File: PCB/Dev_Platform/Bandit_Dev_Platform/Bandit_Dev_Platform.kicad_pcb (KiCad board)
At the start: 4 copper layers, 63.5 x 31.8 mm, 126 parts, among them J12 Conn_01x02_Pin, J5 BNC, J6 BNC, P1 USB_C_Plug_USB2.0, SW1 SW_SPST, U1 AD7253, U10 OPA1664, U11 XC6206PxxxMR, U2 RP2040, U4 NCP164ASNADJT1G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

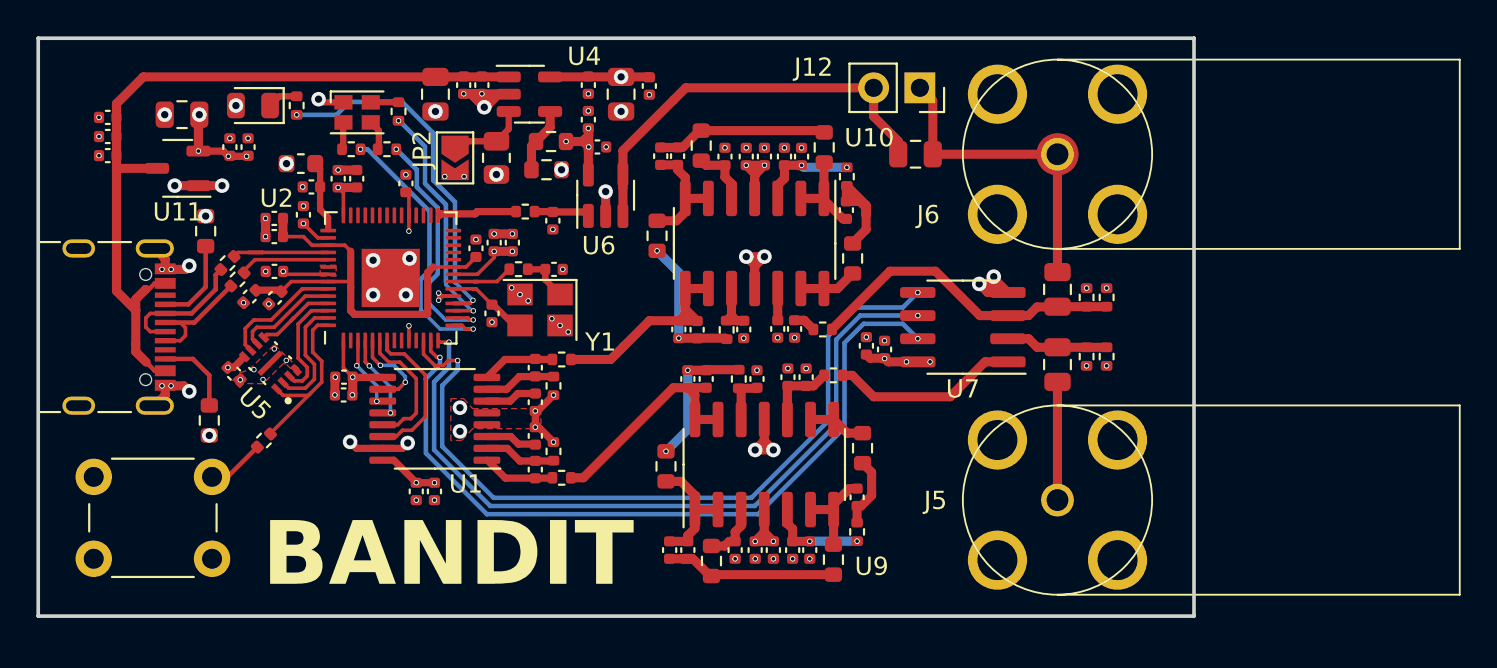
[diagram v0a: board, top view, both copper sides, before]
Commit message: Added filter test board
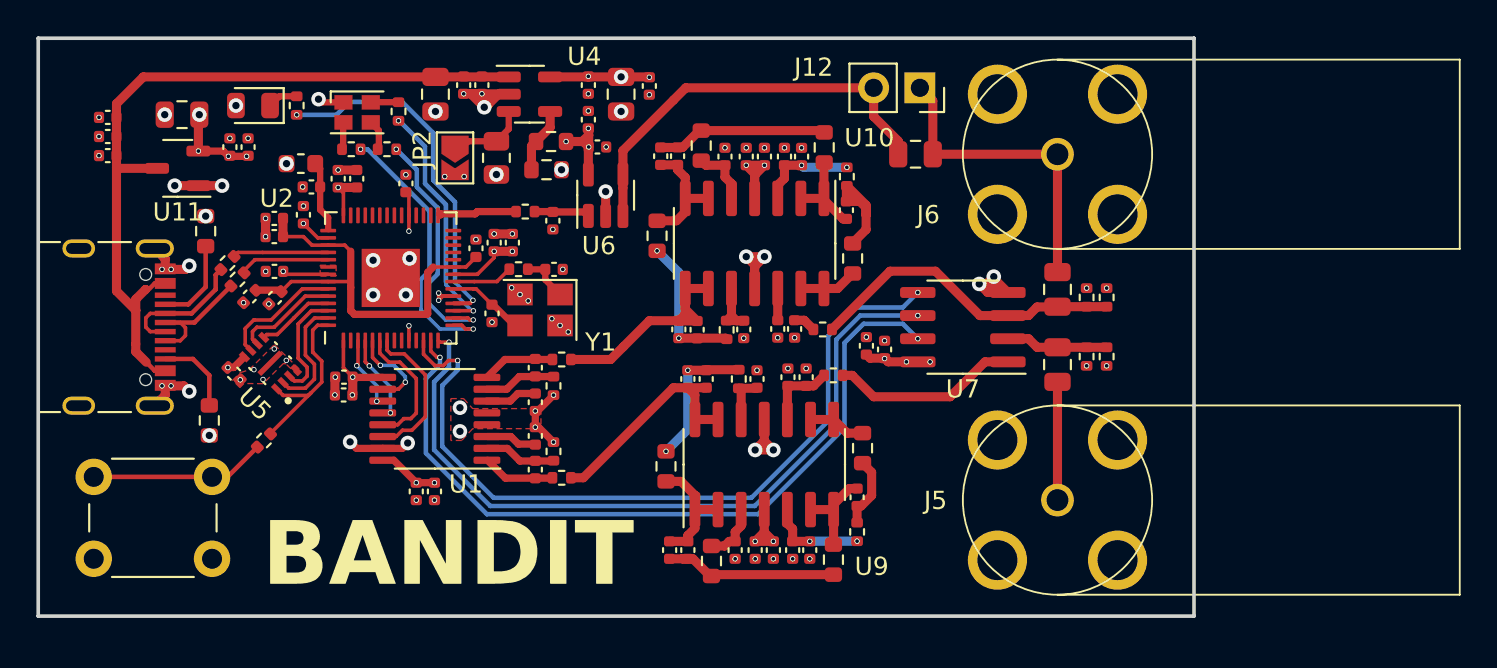
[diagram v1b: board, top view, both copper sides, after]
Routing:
- net GND: track 45.6 -> 59.5 mm
- net Net-(SW1-A): track 3.17 -> 9.67 mm
- net /USB_D-: track 6.04 -> 5.26 mm
- net VDDA: track 25.2 -> 25.3 mm, vias 15 -> 17

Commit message: Dev platform and Filter Test pcb polished, ordered
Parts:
- removed JP2: SolderJumper_2_Open, Jumper:SolderJumper-2_P1.3mm_Open_TrianglePad1.0x1.5mm
- added C12: 100n, Capacitor_SMD:C_0402_1005Metric, F.Cu at (49.7, 41.4)
- added C15: 100n, Capacitor_SMD:C_0402_1005Metric, F.Cu at (49.7, 40.4)
- added C17: 10u, Capacitor_SMD:C_0402_1005Metric, F.Cu at (51.4, 44.1)
- added C18: 10u, Capacitor_SMD:C_0402_1005Metric, F.Cu at (51.4, 37.6)
- added C3: 100n, Capacitor_SMD:C_0402_1005Metric, F.Cu at (68.1, 43.3)
- added C70: 2u2, Capacitor_SMD:C_0402_1005Metric, F.Cu at (39.2, 28.0)
- added R16: 10k, Resistor_SMD:R_0402_1005Metric, F.Cu at (67.6, 41.8)
- added R17: 10k, Resistor_SMD:R_0402_1005Metric, F.Cu at (68.1, 39.3)
- added R18: 10k, Resistor_SMD:R_0402_1005Metric, F.Cu at (51.1, 42.6)
- added R19: 10k, Resistor_SMD:R_0402_1005Metric, F.Cu at (52.1, 42.6)
- added R20: 10k, Resistor_SMD:R_0402_1005Metric, F.Cu at (51.1, 39.1)
- added R42: 10k, Resistor_SMD:R_0402_1005Metric, F.Cu at (51.4, 36.6)
- C2: value 1u -> 10u
- moved C2 30.4 mm to (68.1, 40.3), turned to 0 degrees
- moved SW1 7.85 mm to (27.6, 37.7), turned to -90 degrees
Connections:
- C2 pad 1: VBUS -> /SIG_IN
- C2 pad 2: GND -> Net-(U7-VOUT)
- R22 pad 1: /SE_SIG_A -> Net-(C18-Pad1)
- R23 pad 1: /SE_SIG_B -> Net-(C17-Pad1)
- R7 pad 2: Net-(JP1-B) -> /VDDA_EN
- U2 pad 24: Net-(J1-Pin_1) -> unconnected-(U2-SWCLK-Pad24)
- U2 pad 25: Net-(J1-Pin_2) -> unconnected-(U2-SWD-Pad25)
- U2 pad 32: Net-(J8-Pin_1) -> /VDDA_EN
- U2 pad 34: Net-(J8-Pin_2) -> unconnected-(U2-GPIO22-Pad34)
- U2 pad 35: Net-(J8-Pin_3) -> unconnected-(U2-GPIO23-Pad35)
- U2 pad 36: Net-(J8-Pin_4) -> unconnected-(U2-GPIO24-Pad36)
- U2 pad 37: Net-(J8-Pin_5) -> unconnected-(U2-GPIO25-Pad37)
- U2 pad 38: Net-(J9-Pin_2) -> unconnected-(U2-GPIO26_ADC0-Pad38)
- U2 pad 39: Net-(J9-Pin_3) -> unconnected-(U2-GPIO27_ADC1-Pad39)
- U2 pad 40: Net-(J9-Pin_4) -> unconnected-(U2-GPIO28_ADC2-Pad40)
- U2 pad 41: Net-(J9-Pin_5) -> unconnected-(U2-GPIO29_ADC3-Pad41)
- U4 pad 3: Net-(JP1-B) -> /VDDA_EN
- U5 pad 9: GND -> (no net)
- U7 pad 1: /SIG_IN -> Net-(U7-VOUT)
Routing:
- net /VDDA_EN: track 0.00 -> 9.12 mm
- net Net-(U7-VOUT): track 0.00 -> 5.74 mm
- net Net-(SW1-A): track 9.67 -> 5.16 mm
- net /SIG_IN: track 10.4 -> 6.16 mm
- net Net-(JP1-B): track 4.13 -> 0.00 mm
- net Net-(C17-Pad1): track 0.00 -> 3.76 mm
- net Net-(C18-Pad1): track 0.00 -> 3.73 mm
- net GND: track 59.5 -> 63.0 mm, vias 98 -> 103
- net VDDA: track 25.3 -> 28.7 mm, vias 17 -> 20
- net /SE_SIG_A: track 13.1 -> 10.4 mm
- net /SE_SIG_B: track 12.7 -> 10.8 mm
- net /LED_R: track 15.3 -> 16.5 mm
- net +3V3: track 25.7 -> 26.9 mm, vias 19 -> 30
- net /LED_G: track 13.5 -> 14.3 mm
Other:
- board text added: ":p"
- board text added: "<"
- board text added: ">"
- board text added: "Err"
- board text added: "Stat"
- board text added: "V1"

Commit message: Need to update fab, but fixed C70 duplicate issue from version mismatch
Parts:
- renumbered C70 to C75
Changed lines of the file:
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@@
     (property "ki_keywords" "cap capacitor")
     (attr smd)
-    (fp_text reference "C70" (at 0 -1.68 90) (layer "F.SilkS") hide
+    (fp_text reference "C75" (at 0 -1.68 90) (layer "F.SilkS") hide
         (effects (font (size 1 1) (thickness 0.15)))
     )

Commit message: It's workingggggg (mostly)
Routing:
- net Net-(U10D-+): track 2.99 -> 3.91 mm
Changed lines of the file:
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@@
   (segment (start 62.0519 27.0947) (end 64.4273 27.0947) (width 0.5) (layer "B.Cu") (net 18))
   (segment (start 61.9398 26.9826) (end 62.0519 27.0947) (width 0.5) (layer "B.Cu") (net 18))
+  (segment (start 60.63 35.4946) (end 61.5571 35.4946) (width 0.5) (layer "F.Cu") (net 19))
   (segment (start 60.63 33.75) (end 60.63 35.4946) (width 0.5) (layer "F.Cu") (net 19))
   (segment (start 62.59 36) (end 62.0846 35.4946) (width 0.5) (layer "F.Cu") (net 19))
